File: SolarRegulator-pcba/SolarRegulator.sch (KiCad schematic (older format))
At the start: 23 parts, among them J1 USB_B_Micro

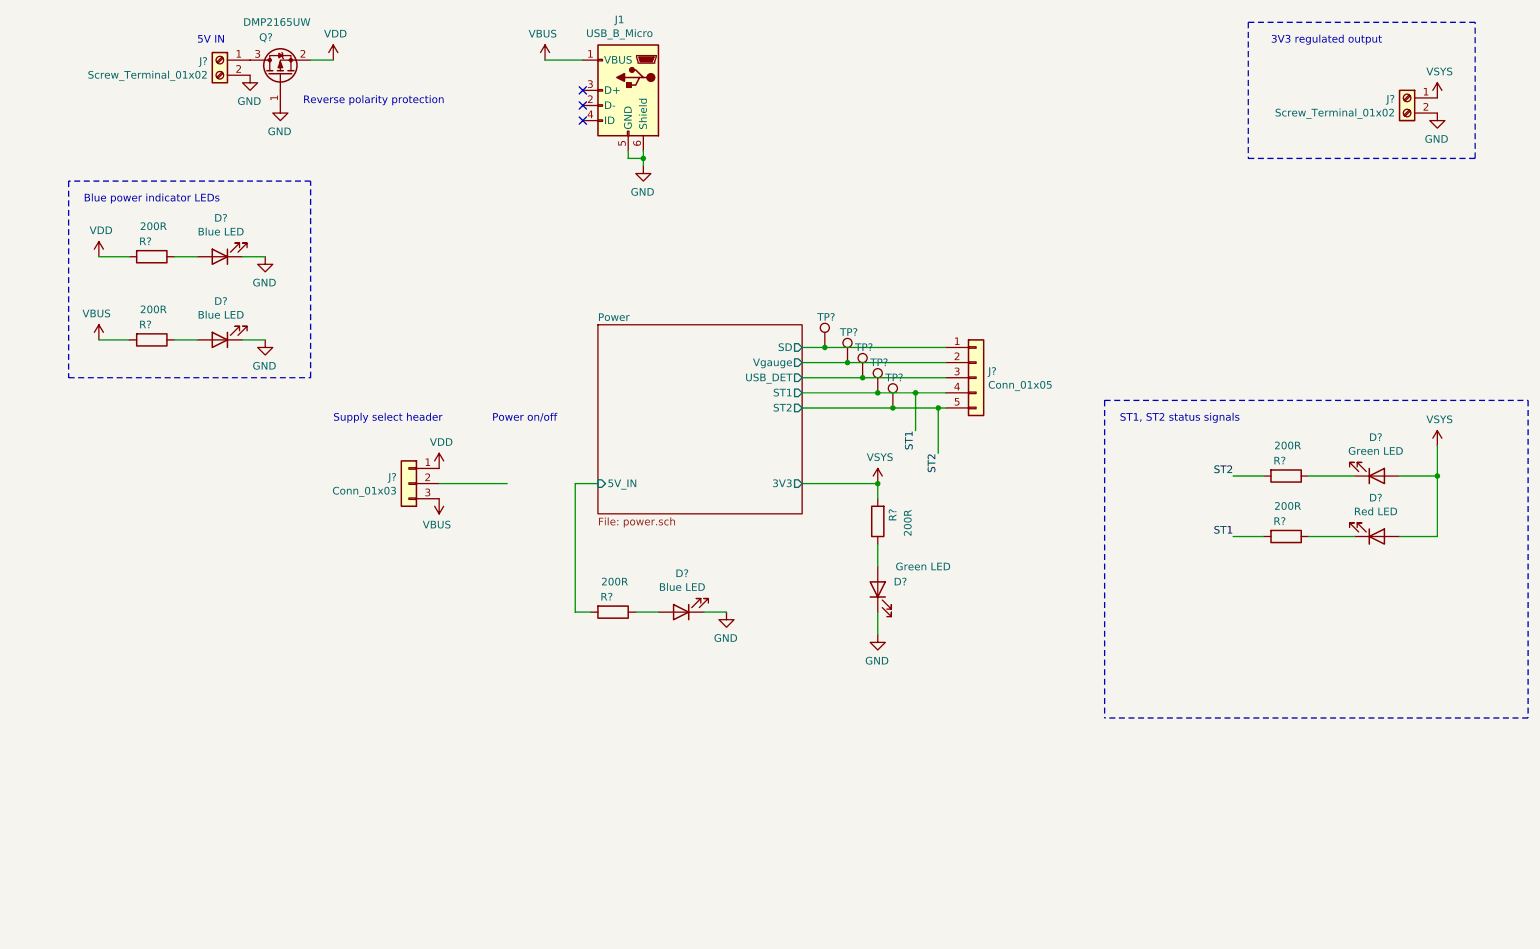
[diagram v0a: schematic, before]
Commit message: Add more footprints to schematic and pcb
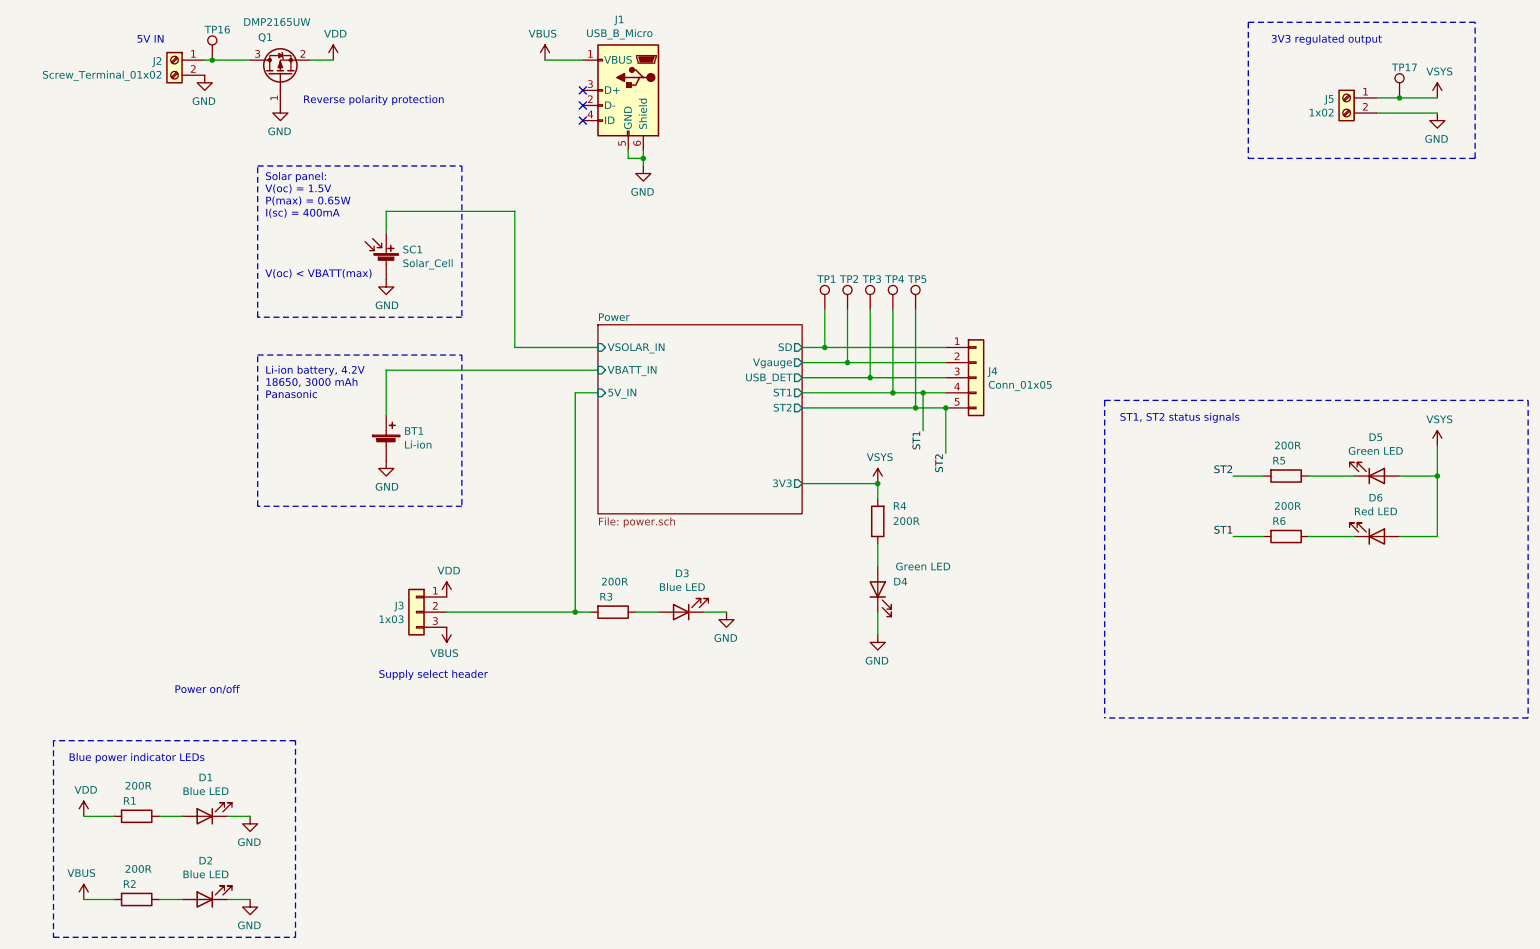
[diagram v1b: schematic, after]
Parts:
- added BT1: Li-ion, TerminalBlock_Phoenix:TerminalBlock_Phoenix_MKDS-1,5-2-5.08_1x02_P5.08mm_Horizontal, symbol Device:Battery_Cell
- added SC1: Solar_Cell, TerminalBlock_Phoenix:TerminalBlock_Phoenix_MKDS-1,5-2-5.08_1x02_P5.08mm_Horizontal, symbol Device:Solar_Cell
- added TP16, TP17: TestPoint, TestPoint:TestPoint_Pad_D1.0mm, symbol Connector:TestPoint
- D1, D2, D3, D4: renamed from D?; footprint LED_THT:LED_D5.0mm -> LED_SMD:LED_1206_3216Metric
- J2: renamed from J?; footprint (none) -> TerminalBlock_Phoenix:TerminalBlock_Phoenix_MKDS-1,5-2-5.08_1x02_P5.08mm_Horizontal
- J3: renamed from J?; value Conn_01x03 -> 1x03; footprint (none) -> Connector_PinHeader_2.54mm:PinHeader_1x03_P2.54mm_Vertical
- J5: renamed from J?; value Screw_Terminal_01x02 -> 1x02; footprint (none) -> TerminalBlock_Phoenix:TerminalBlock_Phoenix_MKDS-1,5-2-5.08_1x02_P5.08mm_Horizontal
- Q1: renamed from Q?; footprint (none) -> Package_TO_SOT_SMD:SOT-323_SC-70_Handsoldering
- TP1, TP2, TP3, TP4, TP5: renamed from TP?; footprint (none) -> TestPoint:TestPoint_Pad_D1.0mm
- gave numbers to parts that had none: 9
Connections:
- net GND: now also BT1.2 (-), SC1.2 (-)
- net Power/5V_IN: now also J3.2 (Pin_2)
- net VDD: now also TP17.1
- net at J2.1 (Pin_1), Q1.3 (D): now also TP16.1
- new net Power/VBATT_IN: BT1.1 (+)
- new net Power/VSOLAR_IN: SC1.1 (+)
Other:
- note added: "Li-ion battery, 4.2V\n18650, 3000 mAh\nPanasonic"
- note added: "Solar panel:\nV(oc) = 1.5V\nP(max) = 0.65W\nI(sc) = 400mA"
- note added: "V(oc) < VBATT(max)"
- moved on the sheet: D1, D2, J2, J3, J5, R1, R2, TP1, TP2, TP3, TP4, TP5

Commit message: Add final footprints, update LED footprints to 1206
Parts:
- D5, D6: footprint LED_THT:LED_D5.0mm -> LED_SMD:LED_1206_3216Metric
- J1: footprint (none) -> Connector_USB:USB_Micro-B_Molex-105017-0001
- J4: footprint (none) -> Connector_PinHeader_2.54mm:PinHeader_1x05_P2.54mm_Vertical
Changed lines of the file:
@@
 F 0 "J1" H 4657 2117 50  0000 C CNN
 F 1 "USB_B_Micro" H 4657 2026 50  0000 C CNN
-F 2 "" H 4750 1600 50  0001 C CNN
+F 2 "Connector_USB:USB_Micro-B_Molex-105017-0001" H 4750 1600 50  0001 C CNN
 F 3 "~" H 4750 1600 50  0001 C CNN
 	1    4600 1650
@@
 F 0 "J4" H 6980 3592 50  0000 L CNN
 F 1 "Conn_01x05" H 6980 3501 50  0000 L CNN
-F 2 "" H 6900 3550 50  0001 C CNN
+F 2 "Connector_PinHeader_2.54mm:PinHeader_1x05_P2.54mm_Vertical" H 6900 3550 50  0001 C CNN
 F 3 "~" H 6900 3550 50  0001 C CNN
 	1    6900 3550
@@
 F 0 "D6" H 9543 4345 50  0000 C CNN
 F 1 "Red LED" H 9543 4436 50  0000 C CNN
-F 2 "LED_THT:LED_D5.0mm" H 9550 4600 50  0001 C CNN
+F 2 "LED_SMD:LED_1206_3216Metric" H 9550 4600 50  0001 C CNN
 F 3 "~" H 9550 4600 50  0001 C CNN
 	1    9550 4600
@@
 F 0 "D5" H 9543 3945 50  0000 C CNN
 F 1 "Green LED" H 9543 4036 50  0000 C CNN
-F 2 "LED_THT:LED_D5.0mm" H 9550 4200 50  0001 C CNN
+F 2 "LED_SMD:LED_1206_3216Metric" H 9550 4200 50  0001 C CNN
 F 3 "~" H 9550 4200 50  0001 C CNN
 	1    9550 4200
